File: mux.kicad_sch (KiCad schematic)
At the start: 22 parts, among them M1 SN74LV4051ADYYR, M10 SN74LV4051ADYYR, M11 SN74LV4051ADYYR, M2 SN74LV4051ADYYR, M3 SN74LV4051ADYYR, M4 SN74LV4051ADYYR, M5 SN74LV4051ADYYR, M6 SN74LV4051ADYYR, M7 SN74LV4051ADYYR, M8 SN74LV4051ADYYR, M9 SN74LV4051ADYYR

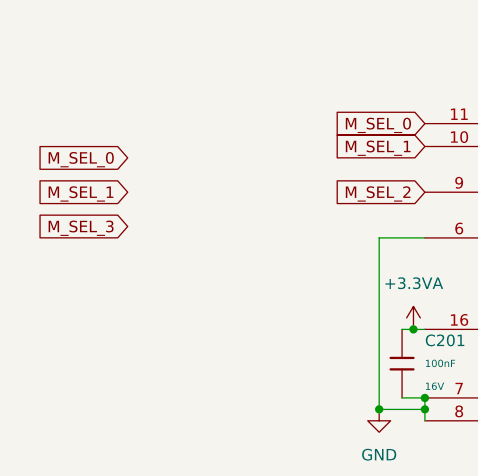
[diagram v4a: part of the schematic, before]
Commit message: add fuse & continue usb
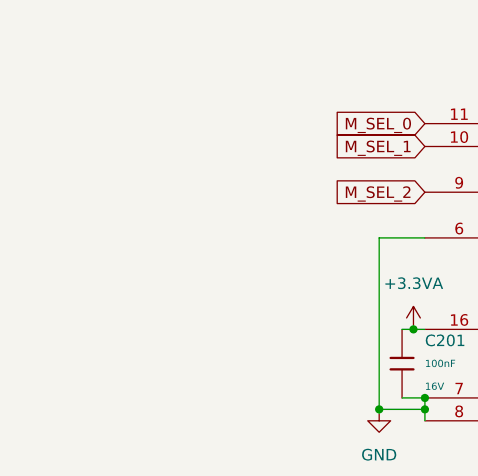
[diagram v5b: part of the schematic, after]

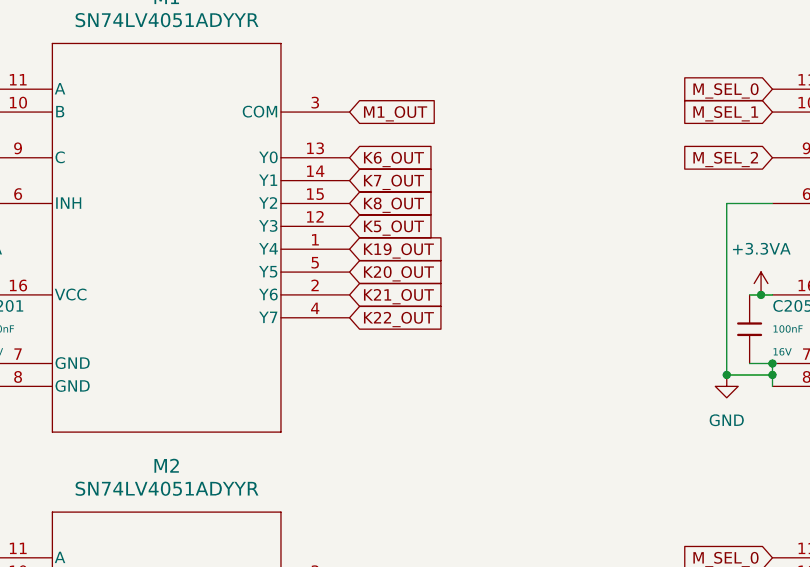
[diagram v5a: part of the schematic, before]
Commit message: start sensor power rail
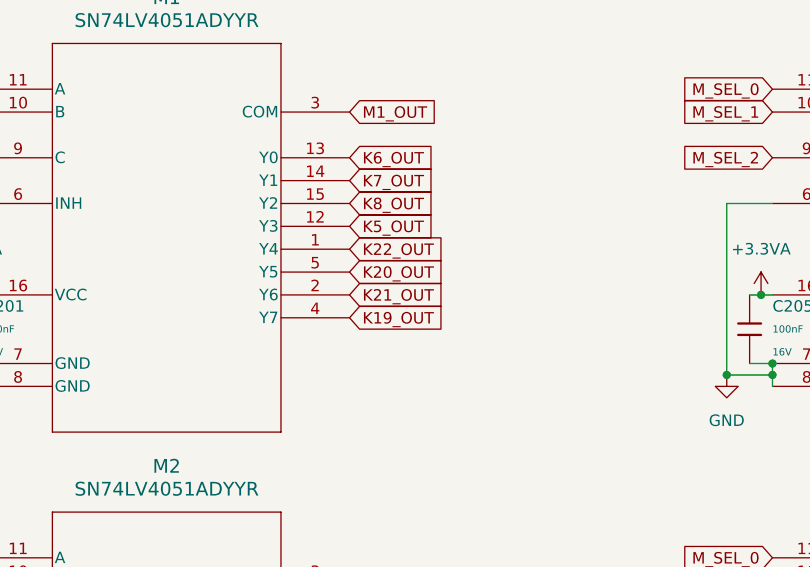
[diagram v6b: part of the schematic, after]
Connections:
- net K19_OUT: now also M1.4 (Y7); no longer M1.1 (Y4)
- net K22_OUT: now also M1.1 (Y4); no longer M1.4 (Y7)

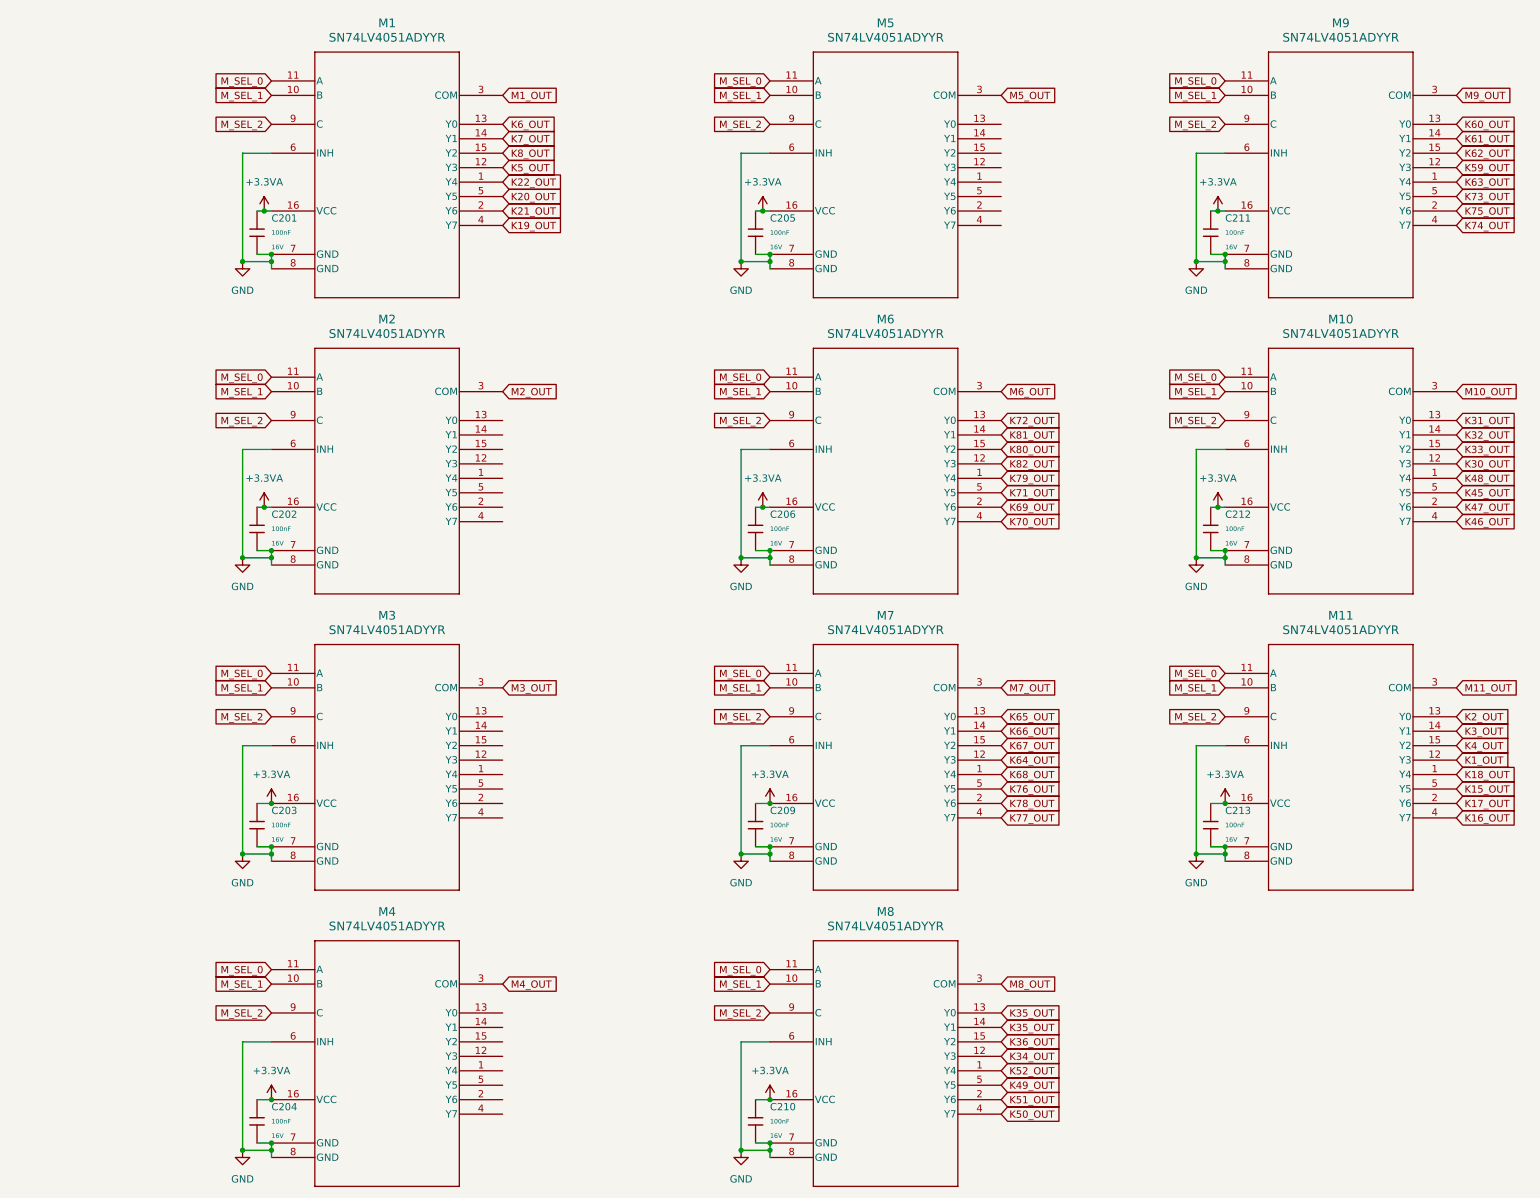
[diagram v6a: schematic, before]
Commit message: start sensor power rail
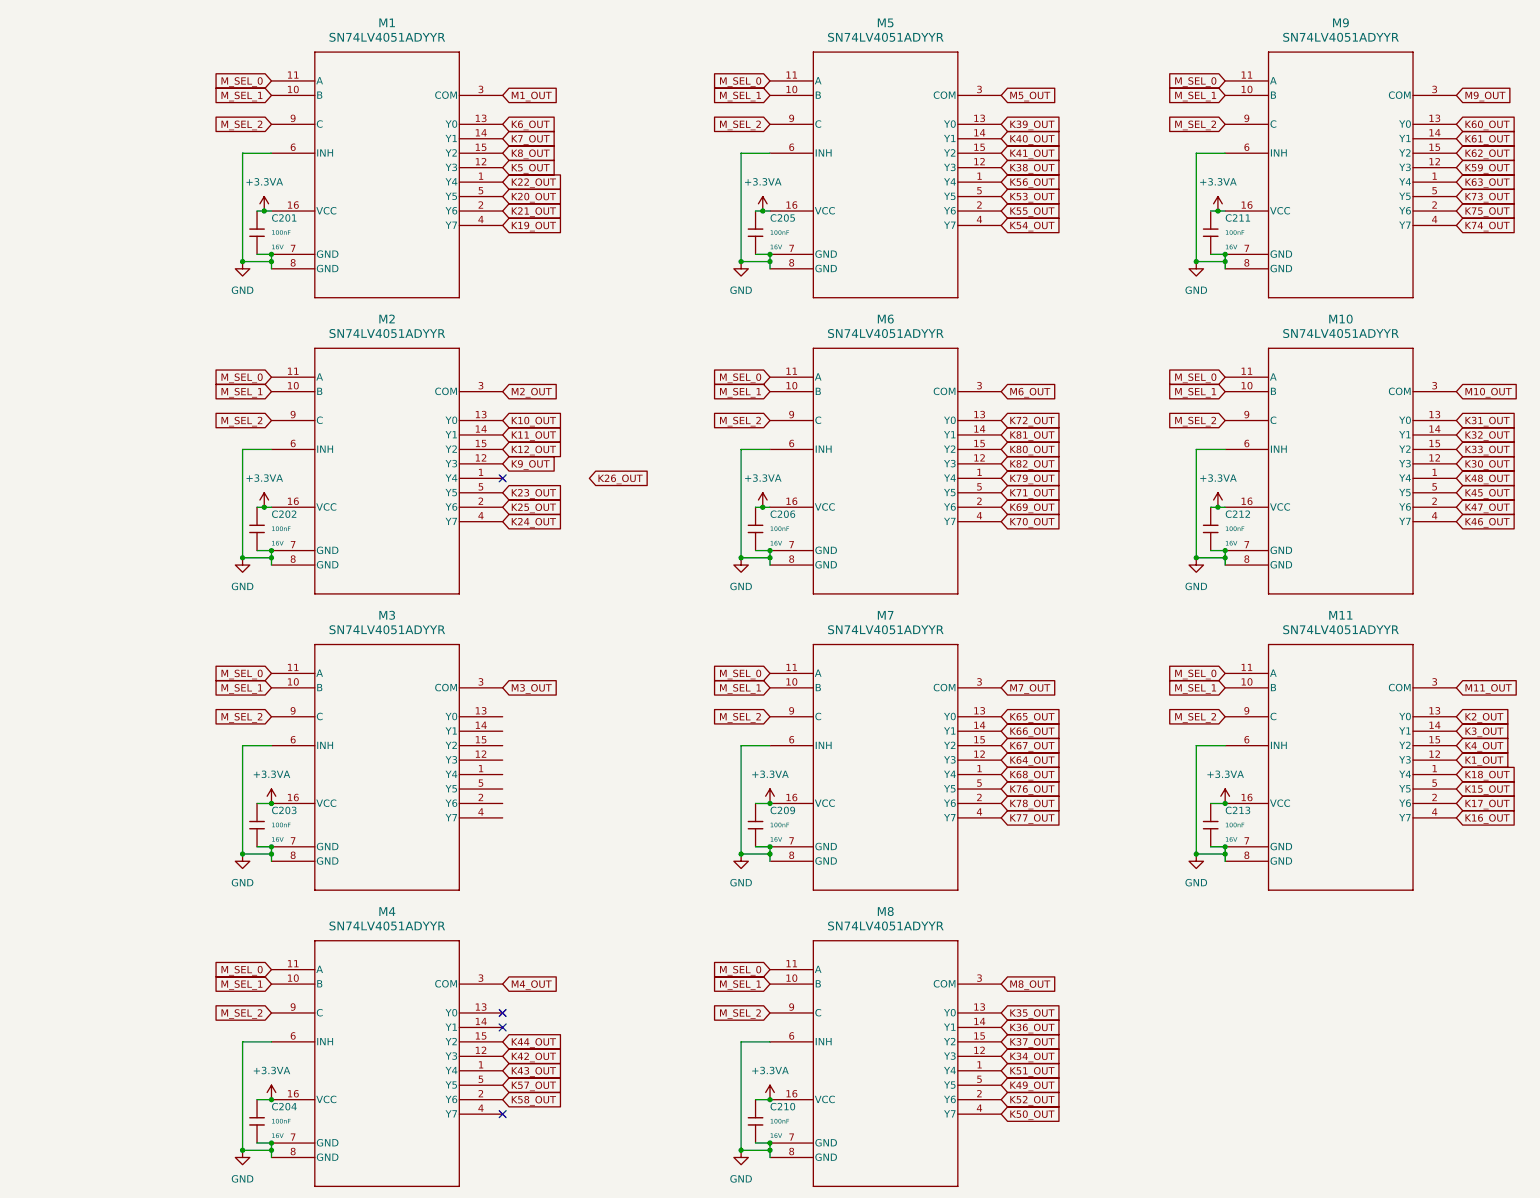
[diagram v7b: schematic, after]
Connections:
- net K35_OUT: no longer M8.14 (Y1)
- net K36_OUT: now also M8.14 (Y1); no longer M8.15 (Y2)
- net K51_OUT: now also M8.1 (Y4); no longer M8.2 (Y6)
- net K52_OUT: now also M8.2 (Y6); no longer M8.1 (Y4)
- net K56_OUT: now reaches M5.1 (Y4)
- net K38_OUT: now reaches M5.12 (Y3)
- net K39_OUT: now reaches M5.13 (Y0)
- net K40_OUT: now reaches M5.14 (Y1)
- net K41_OUT: now reaches M5.15 (Y2)
- net K55_OUT: now reaches M5.2 (Y6)
- net K54_OUT: now reaches M5.4 (Y7)
- net K53_OUT: now reaches M5.5 (Y5)
- net K43_OUT: now reaches M4.1 (Y4)
- net K42_OUT: now reaches M4.12 (Y3)
- net K44_OUT: now reaches M4.15 (Y2)
- net K58_OUT: now reaches M4.2 (Y6)
- net K57_OUT: now reaches M4.5 (Y5)
- net K9_OUT: now reaches M2.12 (Y3)
- net K10_OUT: now reaches M2.13 (Y0)
- net K11_OUT: now reaches M2.14 (Y1)
- net K12_OUT: now reaches M2.15 (Y2)
- net K25_OUT: now reaches M2.2 (Y6)
- net K24_OUT: now reaches M2.4 (Y7)
- net K23_OUT: now reaches M2.5 (Y5)
- new net K37_OUT: M8.15 (Y2)
- no-connect marks 0 -> 4

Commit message: continue sensor out
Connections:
- net K26_OUT: now also M3.5 (Y5)
- net K29_OUT: now reaches M3.1 (Y4)
- net K13_OUT: now reaches M3.12 (Y3)
- net K14_OUT: now reaches M3.15 (Y2)
- net K28_OUT: now reaches M3.2 (Y6)
- net K27_OUT: now reaches M3.4 (Y7)
- no-connect marks 4 -> 6
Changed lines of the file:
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@@
 		(at 69.85 195.58)
 	)
+	(no_connect
+		(at 69.85 140.97)
+	)
+	(no_connect
+		(at 69.85 143.51)
+	)
 	(wire
 		(pts
@@
 		)
 	)
+	(global_label "K13_OUT"
+		(shape input)
+		(at 69.85 148.59 0)
+		(fields_autoplaced yes)
+		(effects
+			(font
+				(size 1.27 1.27)
+			)
+			(justify left)
+		)
+		(property "Intersheetrefs" "${INTERSHEET_REFS}"
+			(at 81.1204 148.59 0)
+			(effects
+				(font
+					(size 1.27 1.27)
+				)
+				(justify left)
+				(hide yes)
+			)
+		)
+	)
 	(global_label "K34_OUT"
 		(shape input)
@@
 		)
 	)
+	(global_label "K27_OUT"
+		(shape input)
+		(at 69.85 158.75 0)
+		(fields_autoplaced yes)
+		(effects
+			(font
+				(size 1.27 1.27)
+			)
+			(justify left)
+		)
+		(property "Intersheetrefs" "${INTERSHEET_REFS}"
+			(at 81.1204 158.75 0)
+			(effects
+				(font
+					(size 1.27 1.27)
+				)
+				(justify left)
+				(hide yes)
+			)
+		)
+	)
 	(global_label "M_SEL_1"
 		(shape input)
@@
 		)
 	)
+	(global_label "K28_OUT"
+		(shape input)
+		(at 69.85 156.21 0)
+		(fields_autoplaced yes)
+		(effects
+			(font
+				(size 1.27 1.27)
+			)
+			(justify left)
+		)
+		(property "Intersheetrefs" "${INTERSHEET_REFS}"
+			(at 81.1204 156.21 0)
+			(effects
+				(font
+					(size 1.27 1.27)
+				)
+				(justify left)
+				(hide yes)
+			)
+		)
+	)
 	(global_label "M_SEL_1"
 		(shape input)
@@
 		)
 	)
+	(global_label "K14_OUT"
+		(shape input)
+		(at 69.85 146.05 0)
+		(fields_autoplaced yes)
+		(effects
+			(font
+				(size 1.27 1.27)
+			)
+			(justify left)
+		)
+		(property "Intersheetrefs" "${INTERSHEET_REFS}"
+			(at 81.1204 146.05 0)
+			(effects
+				(font
+					(size 1.27 1.27)
+				)
+				(justify left)
+				(hide yes)
+			)
+		)
+	)
 	(global_label "K45_OUT"
 		(shape input)
@@
 		)
 	)
+	(global_label "K26_OUT"
+		(shape input)
+		(at 69.85 153.67 0)
+		(fields_autoplaced yes)
+		(effects
+			(font
+				(size 1.27 1.27)
+			)
+			(justify left)
+		)
+		(property "Intersheetrefs" "${INTERSHEET_REFS}"
+			(at 81.1204 153.67 0)
+			(effects
+				(font
+					(size 1.27 1.27)
+				)
+				(justify left)
+				(hide yes)
+			)
+		)
+	)
 	(global_label "M3_OUT"
 		(shape input)
@@
 			(effects
 				(font
+					(size 1.27 1.27)
+				)
+				(justify left)
+				(hide yes)
+			)
+		)
+	)
+	(global_label "K29_OUT"
+		(shape input)
+		(at 69.85 151.13 0)
+		(fields_autoplaced yes)
+		(effects
+			(font
+				(size 1.27 1.27)
+			)
+			(justify left)
+		)
+		(property "Intersheetrefs" "${INTERSHEET_REFS}"
+			(at 81.1204 151.13 0)
+			(effects
+				(font
